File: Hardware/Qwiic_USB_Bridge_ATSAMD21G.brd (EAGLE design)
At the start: 25.4 x 39.4 mm, 28 parts, among them J1 QWIIC_RIGHT_ANGLE, J2 QWIIC_RIGHT_ANGLE, J6 USB_A_SMT_MALE, U1 3.3V, U3 ATSAMD21E18A-U

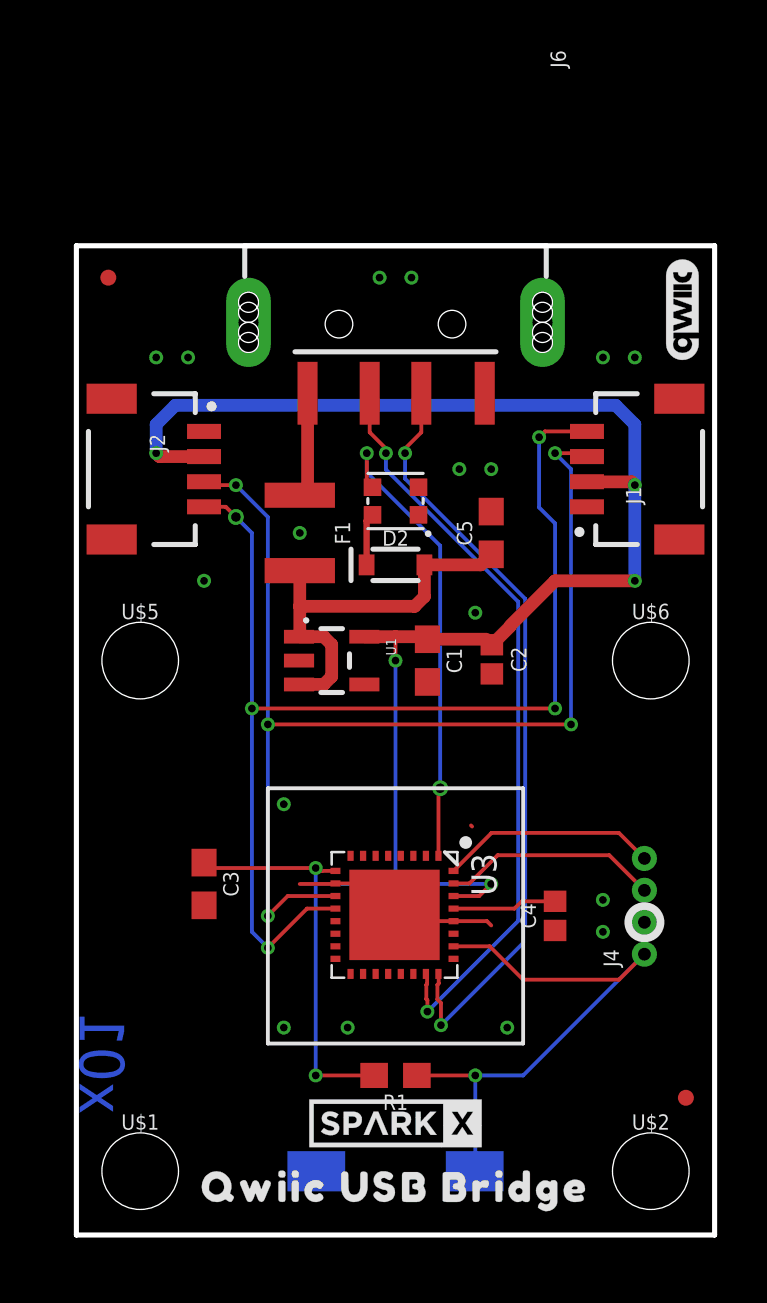
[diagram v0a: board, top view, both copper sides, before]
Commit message: Proto Revision
Swap out ATSAMD21E for 21G TQFP
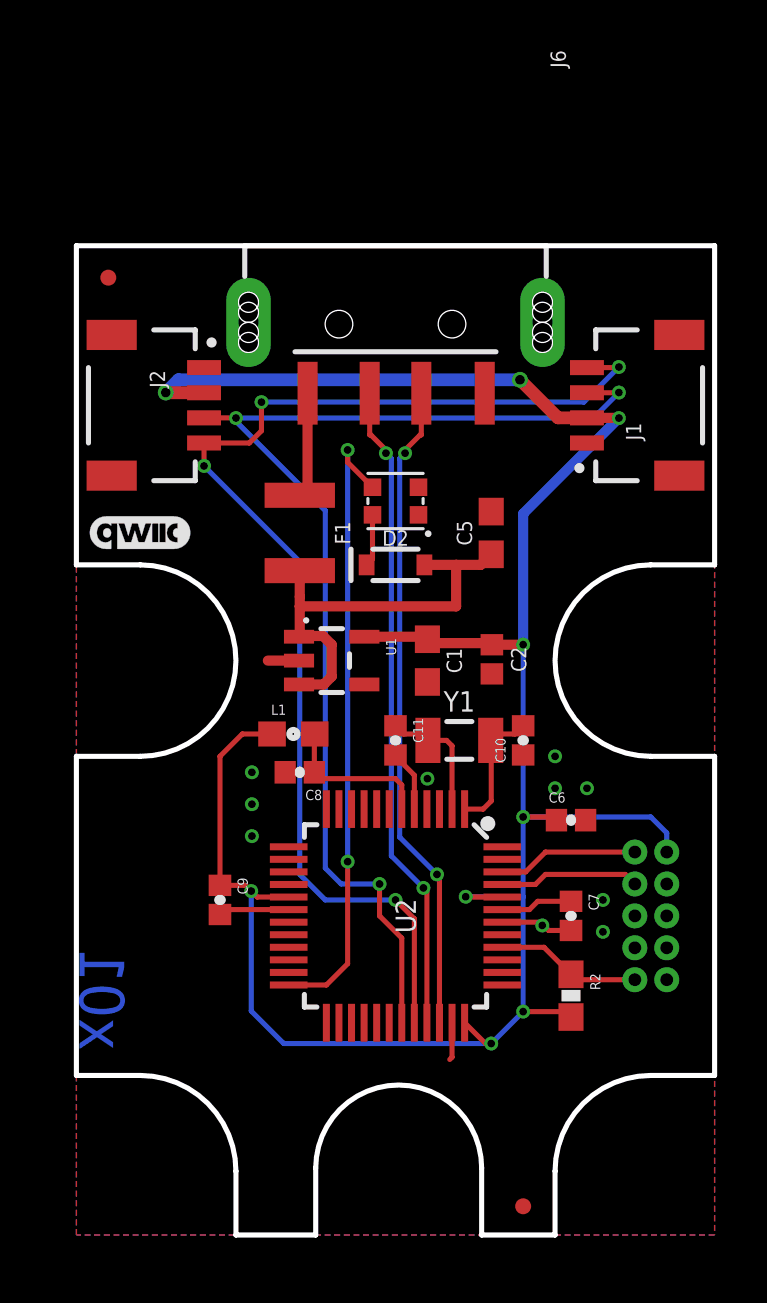
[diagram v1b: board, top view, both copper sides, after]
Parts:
- removed C3: 10uF, SparkFun-Capacitors:0603
- removed C4: 1.0uF, SparkFun-Capacitors:0402
- removed J4: (no value), SparkFun-Connectors:1X04_1.27MM_NO_SILK
- removed R1: 10k, SparkFun-Resistors:0603
- removed S1: MOMENTARY-SWITCH-SPST-SMD-6.0X3.5MM, SparkFun-Switches:TACTILE_SWITCH_SMD_6.0X3.5MM
- removed U$1, U$2, U$5, U$6: (no value), SparkFun-Hardware:STAND-OFF-TIGHT
- removed U$3: (no value), output:QWIIC_USB_BRIDGE0
- removed U$4: (no value), SparkX:SPARKX-SMALL
- removed U3: ATSAMD21E18A-U, SparkFun-IC-Microcontroller:QFN-32_SAMD
- added C10, C11: 15pF, samd21-temp:0402-CAP
- added C6, C7, C8, C9: 0.1uF, SparkFun-Capacitors:0402-CAP
- added J3: CORTEX_JTAG_DEBUG_MINIMUM_PTH, SparkFun-Connectors:2X5-PTH-1.27MM
- added L1: FB - 30Ohm, SparkFun-Passives:0603
- added R2: 10K, SparkFun-Resistors:0603-RES
- added U2: ATSAMD21G-A, samd21-temp:TQFP-48
- added Y1: 32.768kHz, samd21-temp:CRYSTAL-SMD-3.2X1.5MM
- moved U$9 23.3 mm to (2.54, 27.9), turned to 0 degrees
- moved FD2 7.78 mm to (17.8, 1.14)
- moved J1 2.54 mm to (20.3, 33.0)
- moved J2 2.54 mm to (5.08, 33.0)
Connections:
- removed net FLASH_CS: U3.PA19
- removed net FLASH_MISO: U3.PA18
- removed net FLASH_MOSI: U3.PA16
- removed net FLASH_SCK: U3.PA17
- removed net MISO: U3.PA05
- removed net MOSI: U3.PA06
- removed net RX: U3.PA23
- removed net SCK: U3.PA07
- removed net TX: U3.PA22
- removed net VDDCORE: C4.2, U3.VDDCORE
- new net N$3: C10.2, U2.1, Y1.P$2
- new net N$4: C11.1, U2.2, Y1.P$1
- new net VDDANA: C8.1, L1.2, U2.6
- new net VDDCORE1: C7.1, U2.43
- net !RESET: now also J3.10, R2.1, U2.40; no longer J4.1, R1.1, S1.1, U3.RES
- net 3.3V: now also C6.1, C9.1, J3.1, L1.1, R2.2, U2.17, U2.36, U2.44; no longer C3.1, R1.2, U3.VDD, U3.VDDIN
- net GND: now also C10.1, C11.2, C6.2, C7.2, C8.2, C9.2, J3.3, J3.5, J3.9, U2.18, U2.35, U2.42, U2.5; no longer C3.2, C4.1, J4.2, S1.2, U3.GND, U3.GNDANA, U3.PAD
- net LED_IN: now also U2.24; no longer U3.PA00
- net SCL: now also U2.32; no longer U3.PA09
- net SDA: now also U2.31; no longer U3.PA08
- net SWCLK: now also J3.4, U2.45; no longer J4.3, U3.PA30
- net SWDIO: now also J3.2, U2.46; no longer J4.4, U3.PA31
- net USB_N: now also U2.33; no longer U3.PA24
- net USB_P: now also U2.34; no longer U3.PA25
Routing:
- net !RESET: track 23.4 -> 5.81 mm, vias 1 -> 0
- net 3.3V: track 77.4 -> 94.8 mm, vias 7 -> 9
- net LED_IN: track 18.7 -> 25.0 mm
- net VDDANA: track 0.00 -> 6.18 mm
- net N$3: track 0.00 -> 5.28 mm, vias 1 -> 0
- net N$4: track 0.00 -> 5.10 mm, vias 1 -> 0
- net USB_P: track 30.9 -> 26.1 mm
- net VDDCORE: track 4.16 -> 0.00 mm
- net USB_N: track 30.1 -> 26.0 mm
- net SWCLK: track 8.64 -> 5.60 mm
- net SWDIO: track 8.64 -> 5.60 mm
- net VDDCORE1: track 0.00 -> 2.87 mm
- net GND: track 8.38 -> 10.9 mm, vias 0 -> 10
- net VIN: track 16.0 -> 17.5 mm
- net SDA: track 46.5 -> 45.9 mm, vias 5 -> 3
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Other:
- outline, holes or cut-outs redrawn

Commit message: Updating to build version
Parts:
- removed L1: FB - 30Ohm, SparkFun-Passives:0603
- added J4: (no value), SparkFun-Connectors:1X04_NO_SILK
- added U$1: (no value), output:#_A1#0
- added U$2: (no value), output:#_A2#0
- added U$3: (no value), output:#_D11#0
- added U$4: (no value), output:#_D10#0
- C10, C11: device samd21-temp:0402-CAP -> SparkFun-Capacitors:0603
- C2: device SparkFun-Capacitors:0402 -> SparkFun-Capacitors:0603
- C6, C7, C8, C9: device SparkFun-Capacitors:0402-CAP -> SparkFun-Capacitors:0603
- R2: value 10K -> 10k; device SparkFun-Resistors:0603-RES -> SparkFun-Resistors:0603
- U2: device samd21-temp:TQFP-48 -> SparkFun-IC-Microcontroller:TQFP-48
- Y1: device samd21-temp:CRYSTAL-SMD-3.2X1.5MM -> SparkFun-Clocks:CRYSTAL-SMD-3.2X1.5MM
- moved D1 26.7 mm to (12.7, 2.54)
- moved U$9 22.6 mm to (22.9, 37.8)
- moved D2 21.6 mm to (12.7, 5.08)
- moved C5 9.16 mm to (8.89, 22.9), turned to 270 degrees
- moved U$7 7.62 mm to (14.6, 12.1)
- moved U$8 7.62 mm to (10.8, 12.1)
- moved U1 5.43 mm to (12.1, 27.9)
- moved C1 5.24 mm to (15.2, 27.9)
- moved C2 5.18 mm to (17.8, 27.9)
- moved C10 3.42 mm to (16.5, 22.9), turned to 270 degrees
- moved FRAME2 2.54 mm to (-7.62, -11.4)
- moved C11 1.65 mm to (11.0, 19.7), turned to 180 degrees
- moved C8 1.42 mm to (7.62, 19.1), turned to 90 degrees
- moved F1 1.42 mm to (7.62, 27.3)
- moved R2 0.63 mm to (19.7, 8.89), turned to 180 degrees
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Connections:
- removed net VDDANA: C8.1, L1.2, U2.6
- new net A1: J4.4, U2.7
- new net A2: J4.3, U2.8
- new net D10: J4.1, U2.27
- new net D11: J4.2, U2.25
- net 3.3V: now also C8.1, U2.6; no longer L1.1
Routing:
- net A1: track 0.00 -> 16.8 mm, vias 0 -> 1
- net A2: track 0.00 -> 16.6 mm, vias 0 -> 1
- net VIN: track 17.5 -> 33.4 mm, vias 0 -> 2
- net LED_IN: track 25.0 -> 10.4 mm
- net D10: track 0.00 -> 11.4 mm
- net D11: track 0.00 -> 9.91 mm
- net 3.3V: track 94.8 -> 85.2 mm, vias 9 -> 6
- net VDDANA: track 6.18 -> 0.00 mm
- net GND: track 10.9 -> 16.6 mm, vias 10 -> 27
- net USB_N: track 26.0 -> 29.3 mm
- net USB_P: track 26.1 -> 29.4 mm
- net N$2: track 2.09 -> 4.91 mm
- net !RESET: track 5.81 -> 8.40 mm
- net SDA: track 45.9 -> 47.6 mm
- net SCL: track 47.9 -> 49.2 mm
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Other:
- board size 25.4 x 39.4 mm -> 24.9 x 39.4 mm
- board text added: "x02"
- board text removed: "x01"
